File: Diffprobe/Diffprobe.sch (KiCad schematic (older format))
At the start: 7 parts

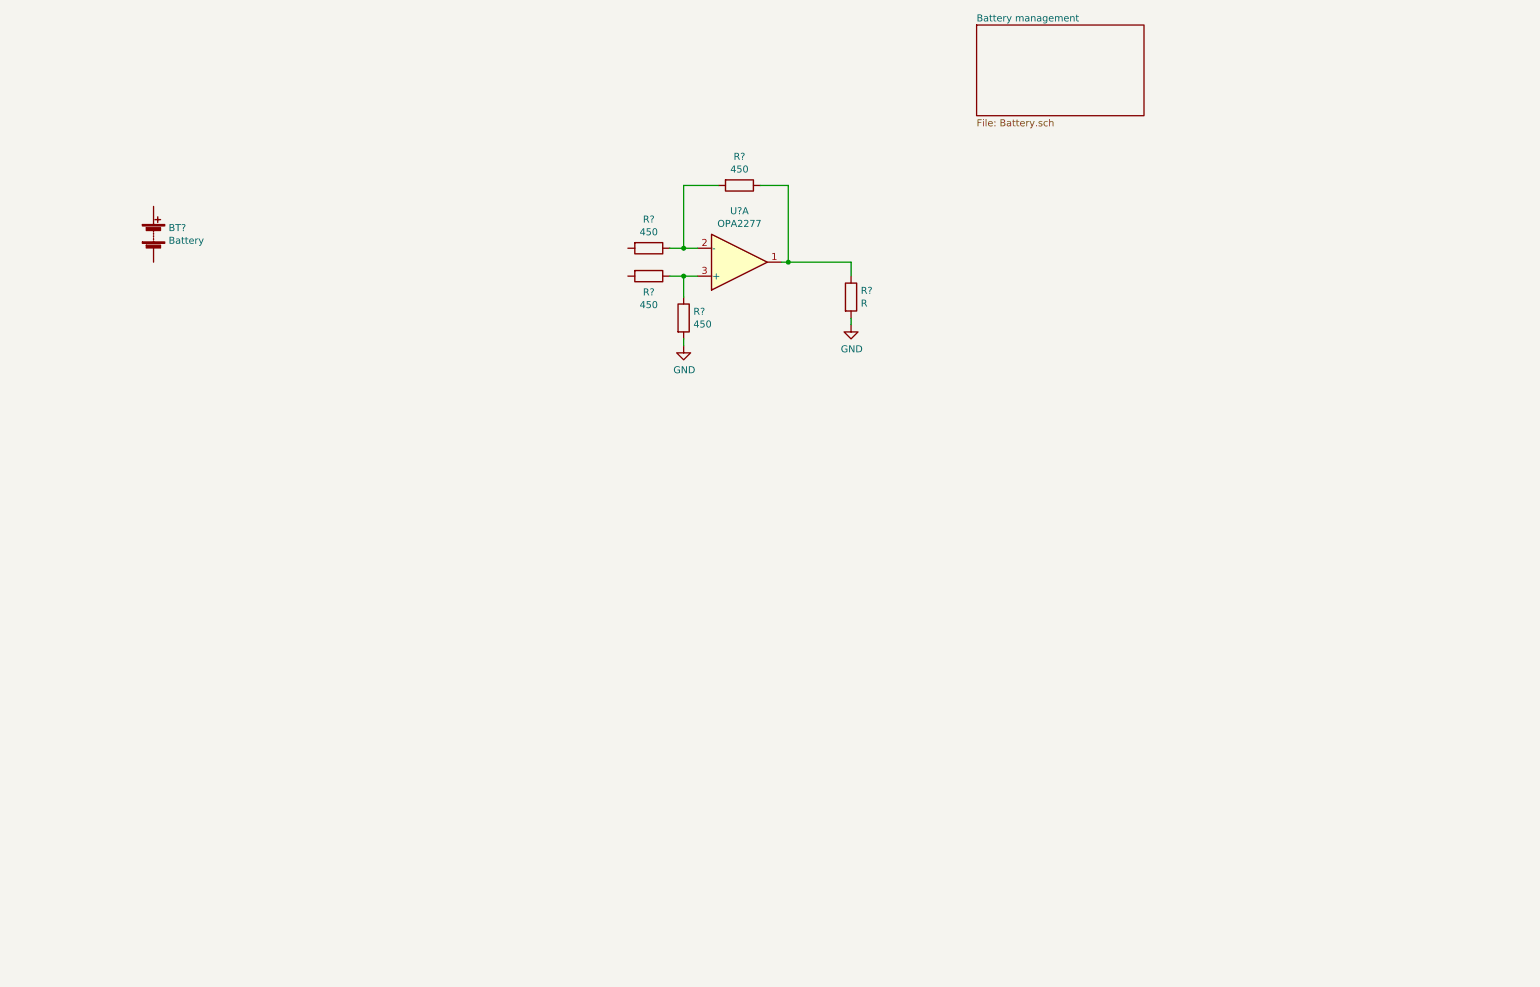
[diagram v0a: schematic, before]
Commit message: differential amplifier + simulations + batterycharger added
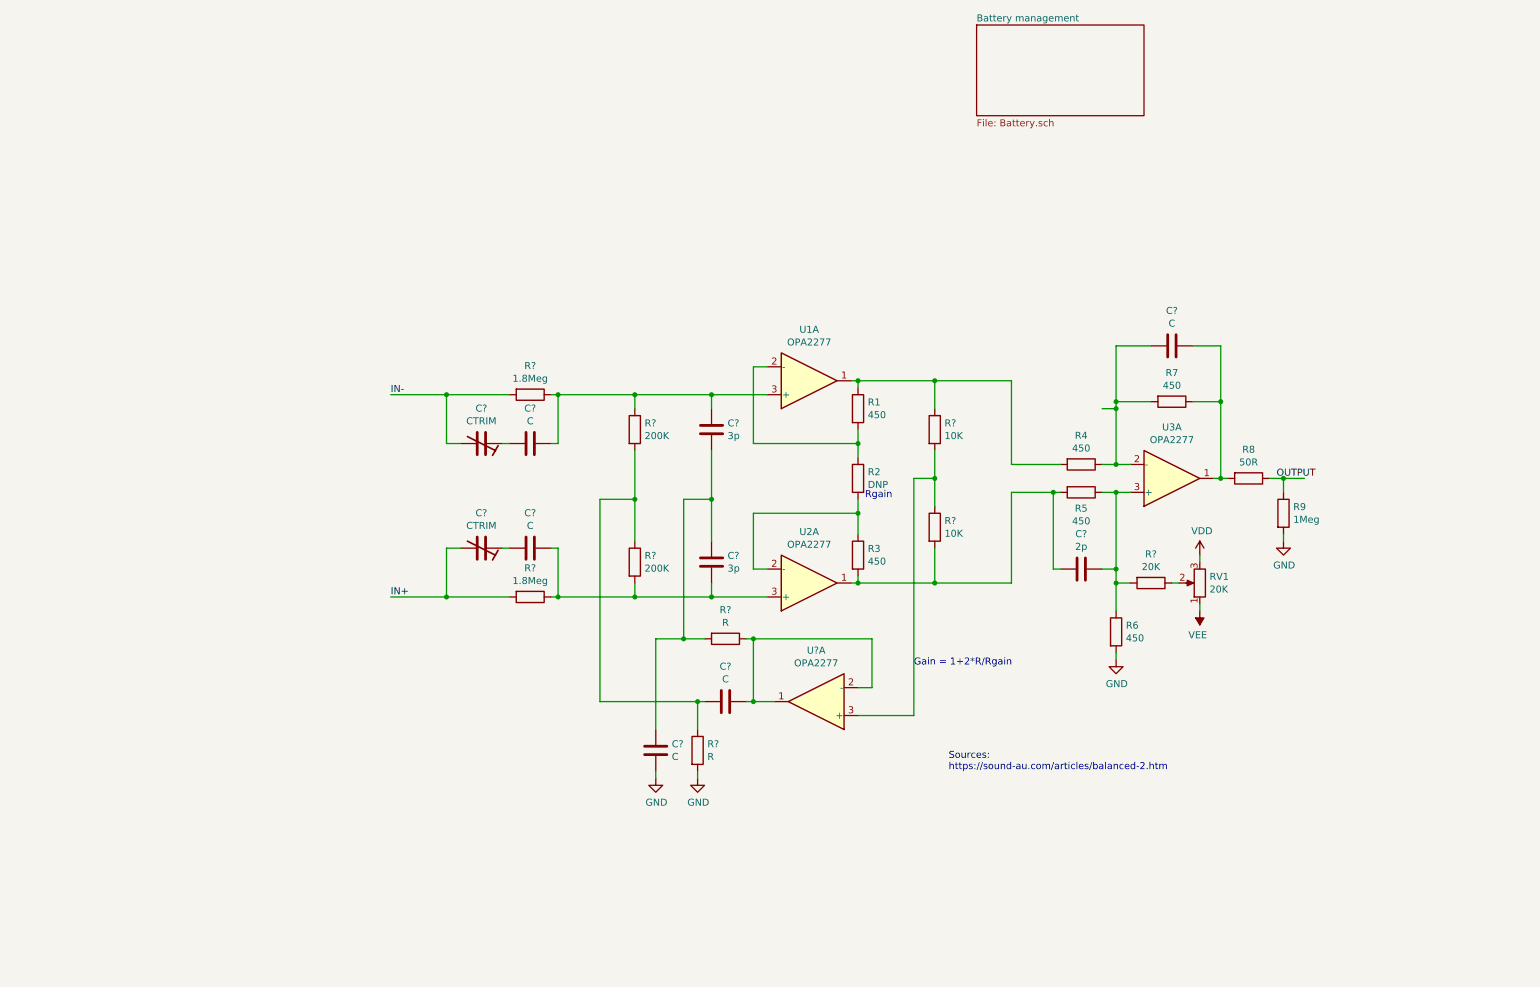
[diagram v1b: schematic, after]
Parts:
- removed BT?: Battery, symbol Device:Battery
- added C? (x5): C, symbol Device:C
- added C? (x2): 3p, symbol Device:C
- added C?: 2p, symbol Device:C
- added C? (x2): CTRIM, symbol Device:CTRIM
- added R1, R3: 450, symbol Device:R
- added R2: DNP, symbol Device:R
- added R8: 50R, symbol Device:R
- added R?: 20K, symbol Device:R
- added R? (x2): 1.8Meg, symbol Device:R
- added R? (x2): 200K, symbol Device:R
- added R? (x2): 10K, symbol Device:R
- added R? (x2): R, symbol Device:R
- added RV1: 20K, symbol Device:R_POT
- added U1, U2, U?: OPA2277, symbol Amplifier_Operational:OPA2277
- R9: renamed from R?; value R -> 1Meg
- gave numbers to parts that had none: 5
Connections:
- net GND: now also C?.2, R?.2
- net at R7.1, U3.1: now also C?.1, R8.2; no longer R9.1
- net at R4.1, R7.2, U3.2 (-): now also C?.2
- net at R5.1, R6.1, U3.3 (+): now also C?.1, R?.2
- net at R4.2: now also R1.1, R?.1, U1.1
- net at R5.2: now also C?.2, R3.2, R?.2, U2.1
- new net: R2.2, R3.1, U2.2 (-)
- new net: C?.1, C?.2, R?.1, R?.2, U2.3 (+)
- new net: R1.2, R2.1, U1.2 (-)
- new net: C?.1, C?.1, R?.1, R?.1, U1.3 (+)
- new net: R?.1, RV1.2
- new net: C?.1, C?.2 (x2)
- new net: C?.1, C?.1, C?.2, R?.2
- new net: C?.2, R?.1, R?.1, R?.2
- new net: R?.1, R?.2, U?.3 (+)
- new net: C?.1, R?.1, U?.1, U?.2 (-)
- new net IN+: C?.2, R?.2
- new net IN-: C?.2, R?.2
- new net OUTPUT: R8.1, R9.1
- new net VDD: RV1.3
- new net VEE: RV1.1
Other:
- note added: "Gain = 1+2*R/Rgain"
- note added: "Rgain\n"
- note added: "Sources:\nhttps://sound-au.com/articles/balanced-2.htm"
- moved on the sheet: R4, R5, R6, R7, R9, U3A

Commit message: more circuitry & simulation added
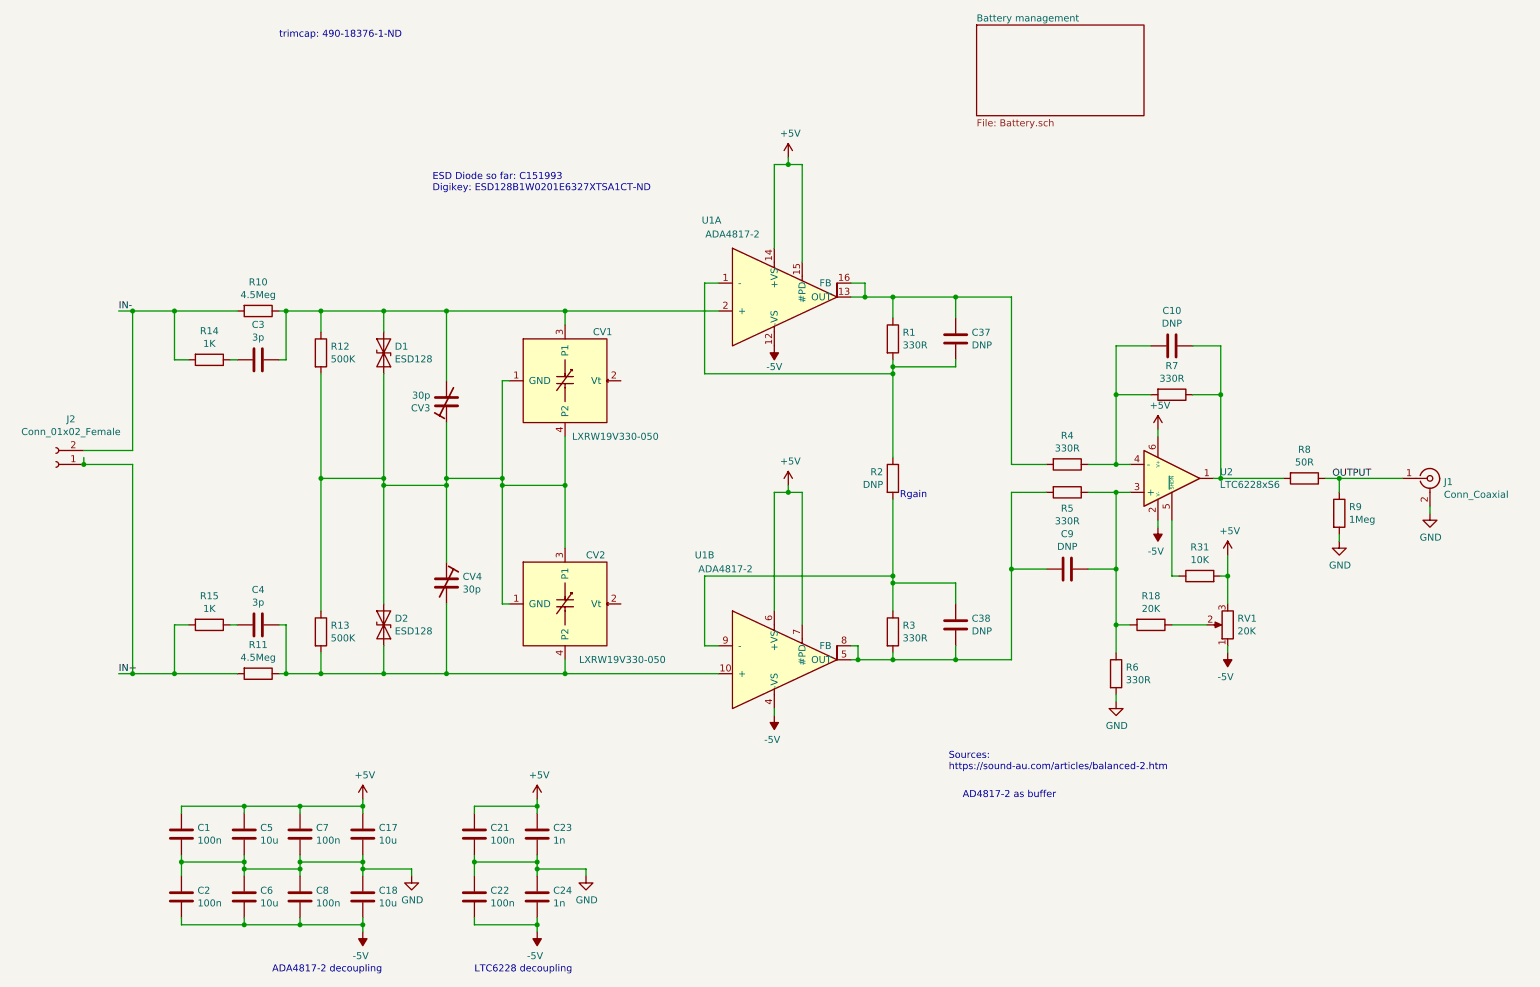
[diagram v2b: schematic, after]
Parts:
- removed C? (x2): 3p, symbol Device:C
- removed C? (x2): CTRIM, symbol Device:CTRIM
- removed C? (x2): C, symbol Device:C
- removed R? (x2): 10K, symbol Device:R
- removed R? (x2): R, symbol Device:R
- removed U1, U2, U3, U?: OPA2277, symbol Amplifier_Operational:OPA2277
- added C1, C2, C22, C7: 100n, Capacitor_SMD:C_0603_1608Metric, symbol Device:C
- added C17, C18, C5, C6: 10u, Capacitor_SMD:C_0805_2012Metric, symbol Device:C
- added C21, C8: 100n, Capacitor_SMD:C_0805_2012Metric, symbol Device:C
- added C23, C24: 1n, Capacitor_SMD:C_0603_1608Metric, symbol Device:C
- added C37, C38: DNP, Resistor_SMD:R_0603_1608Metric, symbol Device:C
- added CV1, CV2: LXRW19V330-050, symbol custom_comps:LXRW19V330-050
- added CV3, CV4: 30p, Capacitor_SMD:C_Trimmer_Murata_TZC3, symbol Device:CTRIM
- added D1, D2: ESD128, Diode_SMD:D_0201_0603Metric, symbol Diode:ESD9B3.3ST5G
- added J1: Conn_Coaxial, Connector_Coaxial:SMA_Wurth_60312002114503_Vertical, symbol Connector:Conn_Coaxial
- added J2: Conn_01x02_Female, symbol Connector:Conn_01x02_Female
- added R14, R15: 1K, Resistor_SMD:R_0603_1608Metric, symbol Device:R
- added R31: 10K, Resistor_SMD:R_0603_1608Metric, symbol Device:R
- added U1: ADA4817-2, Package_CSP:LFCSP-16-1EP_4x4mm_P0.65mm_EP2.4x2.4mm, symbol custom_comps:ADA4817-2
- added U2: LTC6228xS6, Package_TO_SOT_SMD:TSOT-23-6, symbol custom_comps:LTC6228xS6
- C10: renamed from C?; value C -> DNP; footprint (none) -> Capacitor_SMD:C_0805_2012Metric
- C3, C4: renamed from C?; value C -> 3p; footprint (none) -> Capacitor_SMD:C_0603_1608Metric
- C9: renamed from C?; value 2p -> DNP; footprint (none) -> Capacitor_SMD:C_0805_2012Metric
- R1, R3: value 450 -> 330R; footprint (none) -> Resistor_SMD:R_0603_1608Metric
- R10, R11: renamed from R?; value 1.8Meg -> 4.5Meg; footprint (none) -> Resistor_SMD:R_0805_2012Metric
- R12, R13: renamed from R?; value 200K -> 500K; footprint (none) -> Resistor_SMD:R_0805_2012Metric
- R18: renamed from R?; footprint (none) -> Resistor_SMD:R_0805_2012Metric
- R2: footprint (none) -> Resistor_SMD:R_0603_1608Metric
- R4, R5, R6, R7: value 450 -> 330R; footprint (none) -> Resistor_SMD:R_0805_2012Metric
- R8, R9: footprint (none) -> Resistor_SMD:R_0805_2012Metric
- RV1: footprint (none) -> custom_coms:TRIM_3313J-1-103E
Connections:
- net GND: now also C1.2, C17.2, C18.1, C2.1, C21.2, C22.1, C23.2, C24.1, C5.2, C6.1, C7.2, C8.1, J1.2 (Ext)
- net IN+: now also J2.1 (Pin_1), R15.2
- net IN-: now also J2.2 (Pin_2), R14.2
- net OUTPUT: now also J1.1 (In)
- net at C10.1, R7.1, R8.2: now also U2.1
- net at C10.2, R4.1, R7.2: now also U2.4 (-)
- net at C9.1, R18.2, R5.1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: now also U2.3 (+)
- net at R1.1, R4.2: now also C37.1, U1.13 (OUT), U1.16 (FB)
- net at C9.2, R3.2, R5.2: now also C38.2, U1.5 (OUT), U1.8 (FB)
- net at R2.2, R3.1: now also C38.1, U1.9 (-)
- net at C4.1, R11.1, R13.2: now also CV2.4 (P2), CV4.2, D2.2 (A2), U1.10 (+)
- net at R1.2, R2.1: now also C37.2, U1.1 (-)
- net at C3.1, R10.1, R12.1: now also CV1.3 (P1), CV3.2, D1.1 (A1), U1.2 (+)
- net at C3.2: now also R14.1
- net at C4.2: now also R15.1
- net at R12.2, R13.1: now also CV1.1 (GND), CV1.4 (P2), CV2.1 (GND), CV2.3 (P1), CV3.1, CV4.1, D1.2 (A2), D2.1 (A1)
- net VDD renamed +5V
- net +5V: now also C1.1, C17.1, C21.1, C23.1, C5.1, C7.1, R31.2, U1.14 (+VS), U1.15 (#PD), U1.6 (+VS), U1.7 (#PD), U2.6 (V+)
- net VEE renamed -5V
- net -5V: now also C18.2, C2.2, C22.2, C24.2, C6.2, C8.2, U1.12 (-VS), U1.4 (-VS), U2.2 (V-)
- new net: R31.1, U2.5 (~SHDN)
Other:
- note added: "AD4817-2 as buffer\n"
- note added: "ADA4817-2 decoupling"
- note added: "ESD Diode so far: C151993\nDigikey: ESD128B1W0201E6327XTSA1CT-ND"
- note added: "LTC6228 decoupling"
- note added: "trimcap: 490-18376-1-ND\n"
- note removed: "Gain = 1+2*R/Rgain"
- moved on the sheet: C3, C4, C9, R1, R10, R11, R12, R13, R18, R2, R3, R4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

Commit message: readme, 3d files, measurements and more added
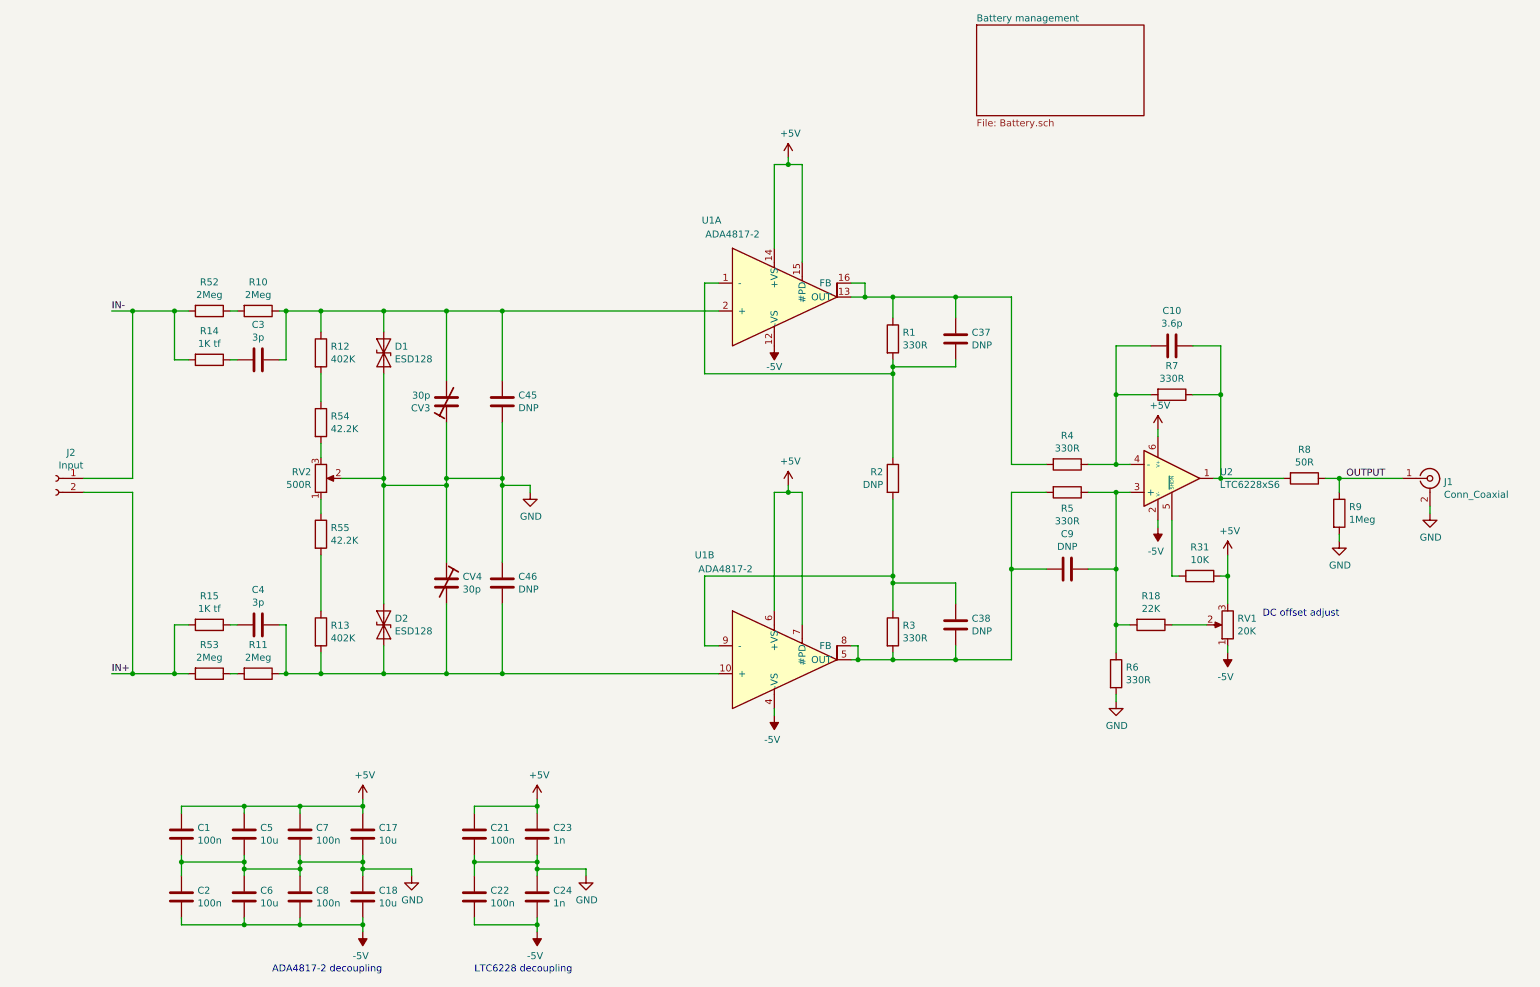
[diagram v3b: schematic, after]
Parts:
- removed CV1, CV2: LXRW19V330-050, symbol custom_comps:LXRW19V330-050
- added C45, C46: DNP, Capacitor_SMD:C_0603_1608Metric, symbol Device:C
- added R52, R53: 2Meg, Resistor_SMD:R_0805_2012Metric, symbol Device:R
- added R54, R55: 42.2K, Resistor_SMD:R_0805_2012Metric, symbol Device:R
- added RV2: 500R, custom_coms:TRIM_3313J-1-103E, symbol Device:R_POT
- C10: value DNP -> 3.6p
- C17, C18, C5, C6: LCSC (none) -> C15850
- C23, C24: LCSC (none) -> C106246
- C3, C4: LCSC (none) -> C527036
- D1, D2: footprint Diode_SMD:D_0201_0603Metric -> Diode_SMD:D_SOD-323; LCSC (none) -> C151993
- J2: value Conn_01x02_Female -> Input; footprint (none) -> custom_coms:probepads
- R1, R3, R4, R5, R6, R7: LCSC (none) -> C328393
- R10, R11: value 4.5Meg -> 2Meg; LCSC (none) -> C306157
- R12, R13: value 500K -> 402K; LCSC (none) -> C706240
- R14, R15: value 1K -> 1K tf; footprint Resistor_SMD:R_0603_1608Metric -> Resistor_SMD:R_0805_2012Metric
- R18: value 20K -> 22K; LCSC (none) -> C114565
- R8: LCSC (none) -> C164002
- R9: LCSC (none) -> C107700
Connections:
- net GND: now also CV3.1, CV4.1, D1.1 (A1), D2.1 (A1), C45.2, C46.1, RV2.2
- net IN+: now also J2.2 (Pin_2), R53.2; no longer J2.1 (Pin_1), R11.2
- net IN-: now also J2.1 (Pin_1), R52.2; no longer J2.2 (Pin_2), R10.2
- net at C3.1, CV3.2, R10.1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: now also D1.2 (A2), C45.1; no longer D1.1 (A1)
- net at C4.1, CV4.2, D2.2 (A2)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: now also C46.2
- new net: R10.2, R52.1
- new net: R11.2, R53.1
- new net: R13.1, R55.2
- new net: R12.2, R54.1
- new net: R54.2, RV2.3
- new net: R55.1, RV2.1
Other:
- note added: "DC offset adjust"
- note removed: "AD4817-2 as buffer\n"
- note removed: "ESD Diode so far: C151993\nDigikey: ESD128B1W0201E6327XTSA1CT-ND"
- note removed: "Rgain\n"
- note removed: "Sources:\nhttps://sound-au.com/articles/balanced-2.htm"
- note removed: "trimcap: 490-18376-1-ND\n"
- moved on the sheet: J2
